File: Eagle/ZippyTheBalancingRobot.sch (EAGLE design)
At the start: 33 parts

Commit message: Update schematic
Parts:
- C5: value (none) -> 470 uF
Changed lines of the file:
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@@
 <part name="SUPPLY11" library="SparkFun-Aesthetics" deviceset="5V" device=""/>
 <part name="SUPPLY12" library="SparkFun-Aesthetics" deviceset="VIN" device=""/>
-<part name="C5" library="adafruit" deviceset="CPOL-US" device="E3.5-8"/>
+<part name="C5" library="adafruit" deviceset="CPOL-US" device="E3.5-8" value="470 uF"/>
 <part name="C6" library="SparkFun-Capacitors" deviceset="CAP" device="PTH" value="0.1 uF"/>
 <part name="RC" library="SparkFun-Connectors" deviceset="M04" device="PTH"/>

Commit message: Add board design
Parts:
- removed R8: 10K, resistor:R-US_0207/10
- added BATTERY: (no value), SparkFun-Connectors:M025MM
- C1, C3: value 47 uF -> 470 uF; device adafruit:CPOL-USE2-5 -> adafruit:CPOL-USE3.5-8
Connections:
- net N$1 renamed R_IN_PWM
- net N$11 renamed LED+
- net N$13 renamed V0
- net N$2 renamed R_IN_A
- net N$3 renamed L_IN_PWM
- net N$4 renamed L_IN_A
- net N$5 renamed L_IN_B
- net N$8 renamed R_IN_B
- removed net N$6: LEFT_MTR.EN/DIAG_A, LEFT_MTR.EN/DIAG_B, R4.1
- removed net N$9: R8.1, RIGHT_MTR.EN/DIAG_A, RIGHT_MTR.EN/DIAG_B
- new net 3V3_PULLUP: LEFT_MTR.EN/DIAG_A, LEFT_MTR.EN/DIAG_B, R4.1, RIGHT_MTR.EN/DIAG_A, RIGHT_MTR.EN/DIAG_B
- net 3.3V: no longer R8.2
- net 5V: now also LEFT_ENC.2, RC.2, RIGHT_ENC.2; no longer LEFT_ENC.3, RC.3, RIGHT_ENC.3
- net D12: now also LEFT_ENC.4; no longer LEFT_ENC.1
- net D2: now also RIGHT_ENC.3; no longer RIGHT_ENC.2
- net D3: now also LEFT_ENC.3; no longer LEFT_ENC.2
- net D4: now also RIGHT_ENC.4; no longer RIGHT_ENC.1
- net D5: now also RC.4; no longer RC.1
- net D6: now also RC.3; no longer RC.2
- net GND: now also BATTERY.1, LEFT_ENC.1, RC.1, RIGHT_ENC.1; no longer LEFT_ENC.4, RC.4, RIGHT_ENC.4
- net VIN: now also BATTERY.2
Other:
- moved on the sheet: BUTTON, LEFT_ENC, R4, RC, RIGHT_ENC

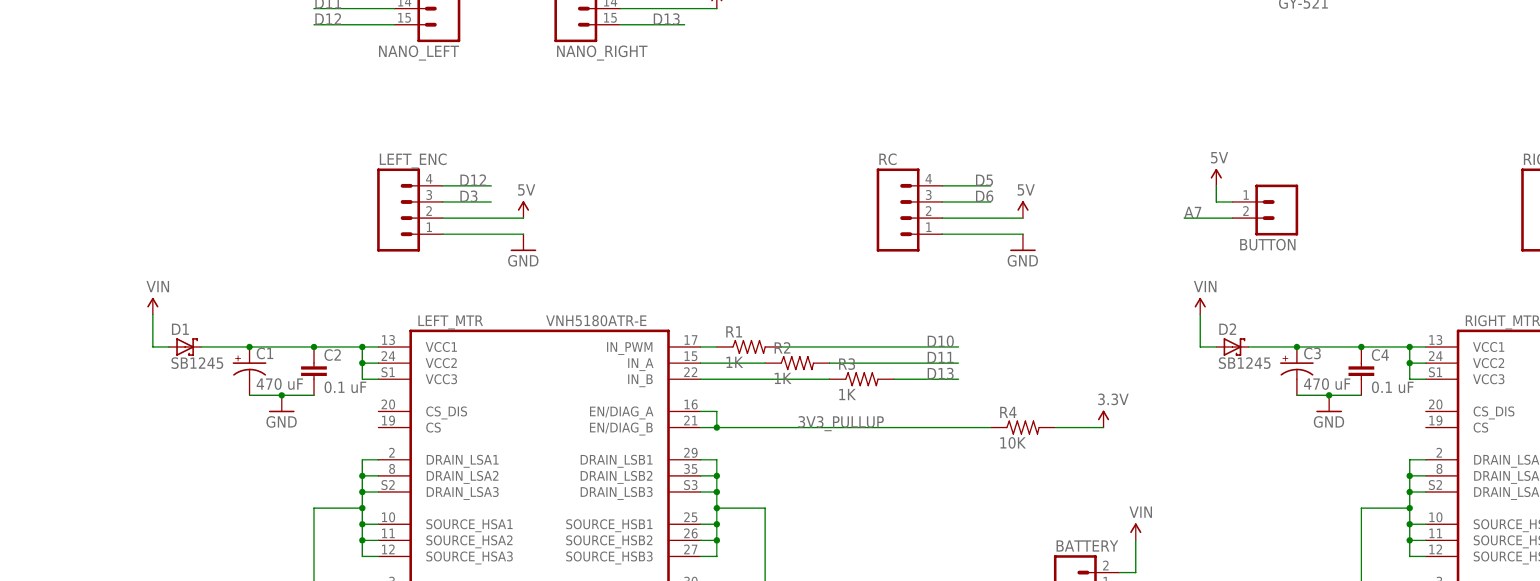
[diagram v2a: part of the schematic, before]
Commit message: Update code for PCB, and fix PCB errors.
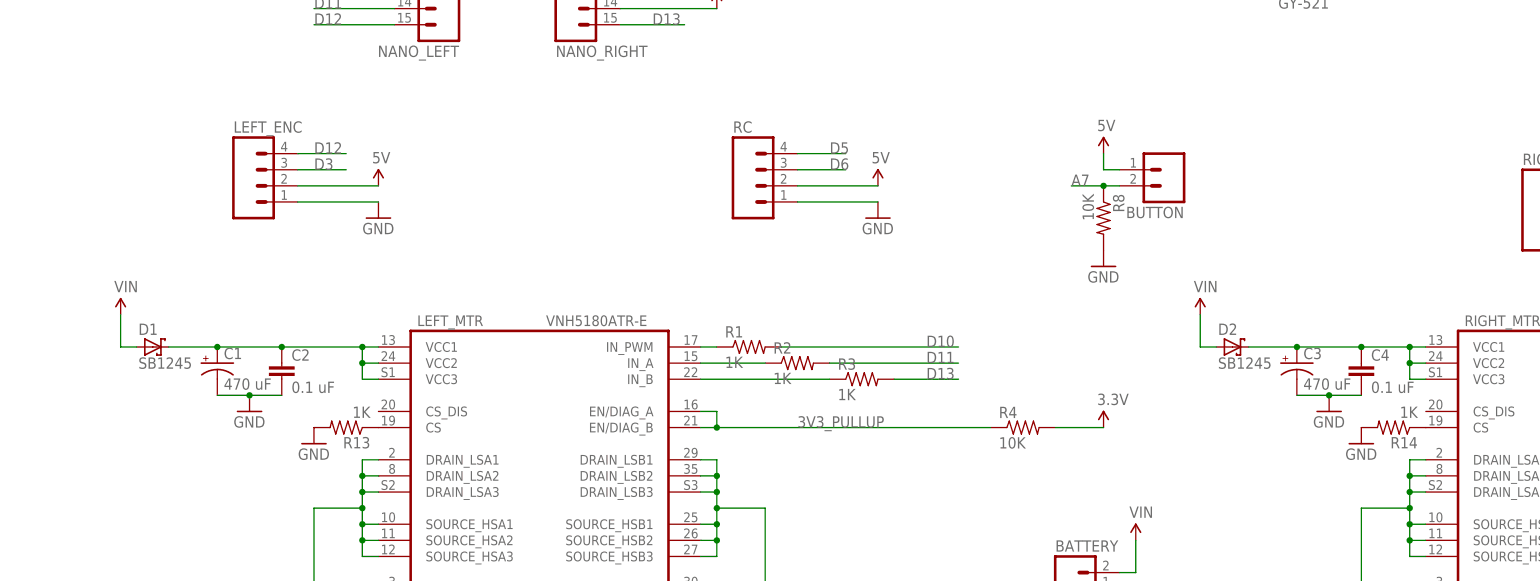
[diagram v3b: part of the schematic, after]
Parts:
- added R13, R14: 1K, resistor:R-US_0207/10
- added R8: 10K, resistor:R-US_0207/10
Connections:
- new net N$1: LEFT_MTR.CS, R13.1
- new net N$3: R14.1, RIGHT_MTR.CS
- net A7: now also R8.1
- net GND: now also R13.2, R14.2, R8.2
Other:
- moved on the sheet: BUTTON, C1, C2, D1, LEFT_ENC, RC
